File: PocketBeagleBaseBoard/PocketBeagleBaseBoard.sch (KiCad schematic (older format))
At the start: 16 parts, among them J1 RJ45, J2 RJ45, P1 POCKETBEAGLE-P1, P2 POCKETBEAGLE-P2, T1 + 15 in -, T2 + 15 out -, U1 TCAN332DR, U2 SN65HVD233-HT

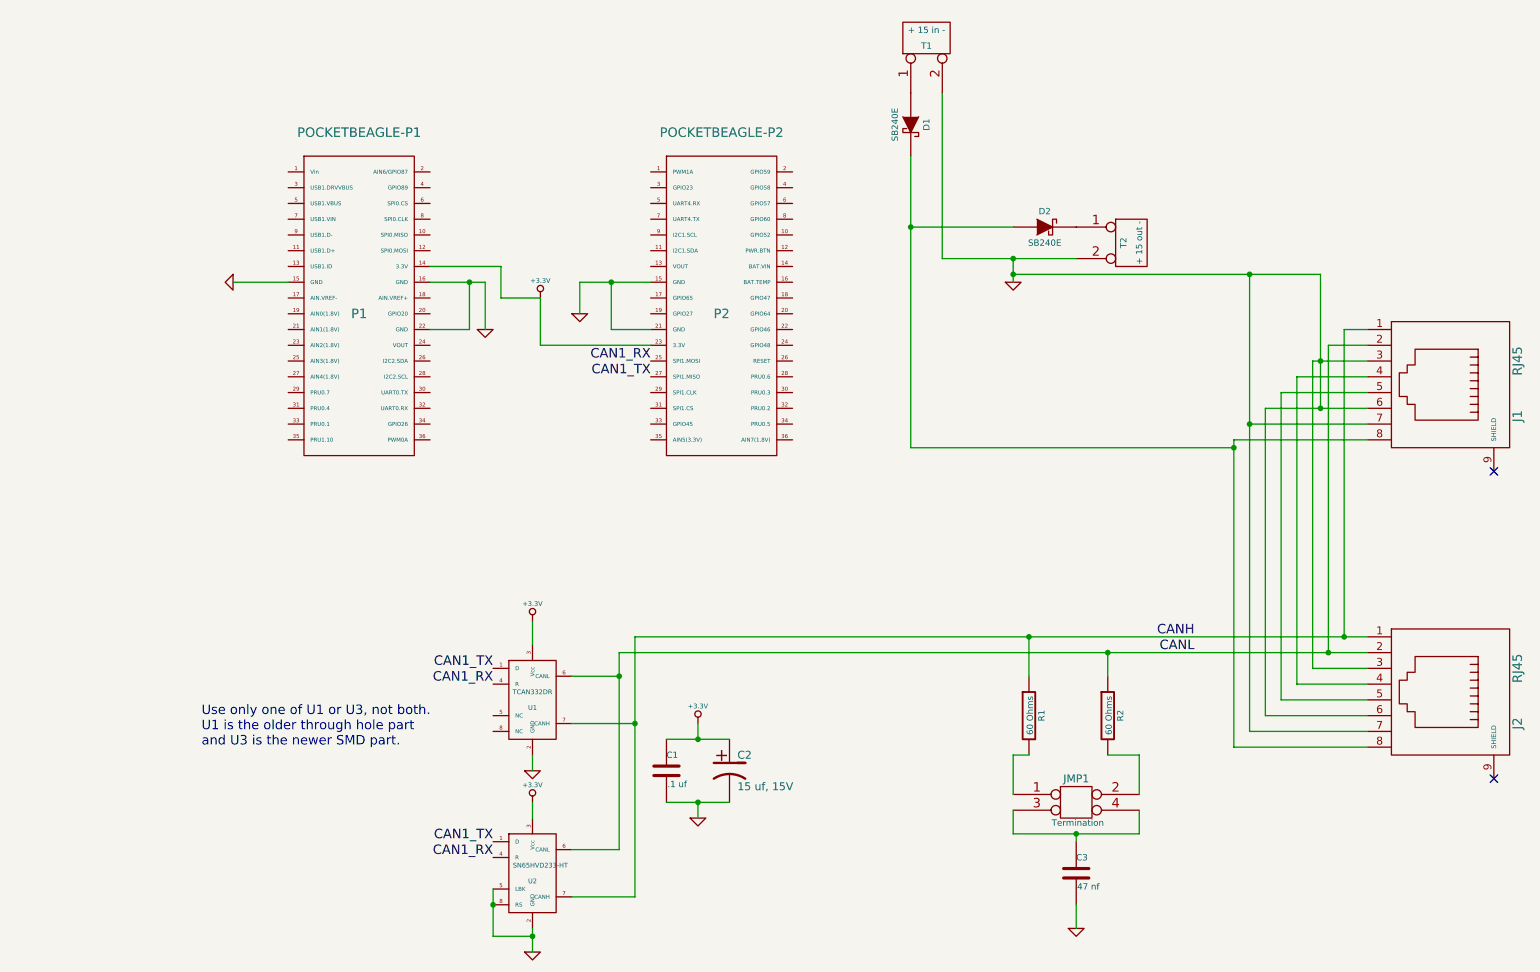
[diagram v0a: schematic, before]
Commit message: Added GPIO, SPI and I2C headers. to PocketBeagleBaseBoard.
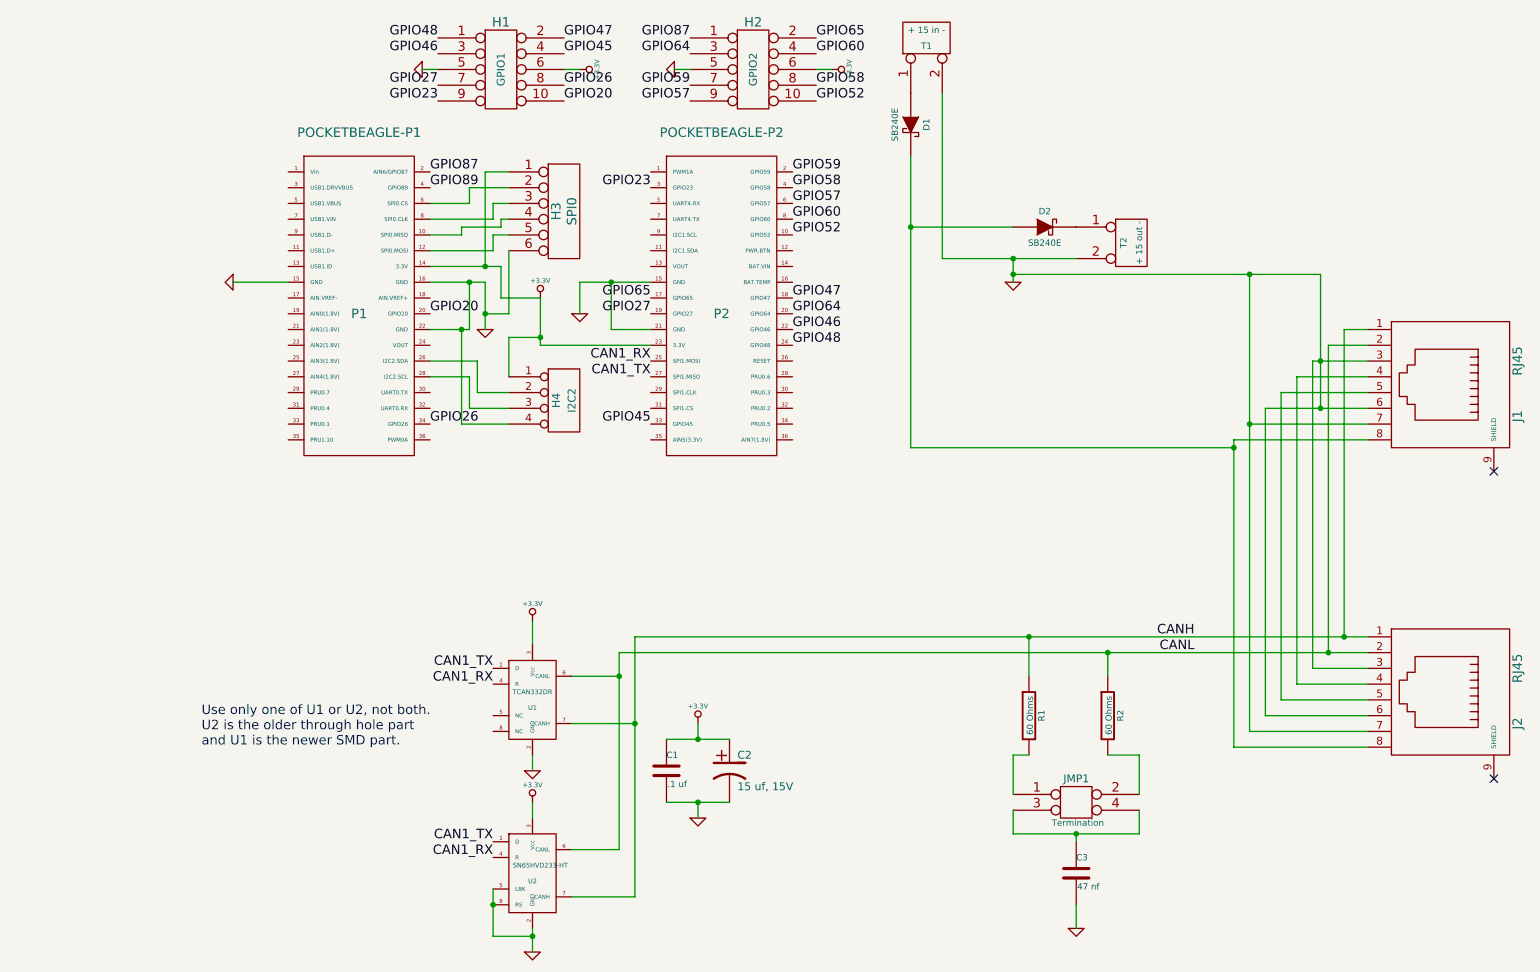
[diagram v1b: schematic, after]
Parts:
- added H1: GPIO1, symbol CONN_5X2
- added H2: GPIO2, symbol CONN_5X2
- added H3: SPI0, symbol CONN_6
- added H4: I2C2, symbol CONN_4
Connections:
- net +3.3V: now also H1.6, H2.6, H3.1, H4.1 (P1)
- net GND: now also H1.5, H2.5, H3.6, H4.4 (P4)
- net at P1.10 (SPI0.MISO): now also H3.4
- net at P1.12 (SPI0.MOSI): now also H3.5
- net GPIO87: now reaches P1.2 (AIN6/GPIO87)
- net GPIO87: now also H2.1
- net GPIO20: now reaches P1.20 (GPIO20)
- net GPIO20: now also H1.10
- net at P1.26 (I2C2.SDA): now also H4.2 (P2)
- net at P1.28 (I2C2.SCL): now also H4.3 (P3)
- net GPIO26: now reaches P1.34 (GPIO26)
- net GPIO26: now also H1.8
- net GPIO89: now reaches P1.4 (GPIO89)
- net at P1.6 (SPI0.CS): now also H3.2
- net at P1.8 (SPI0.CLK): now also H3.3
- net GPIO52: now reaches P2.10 (GPIO52)
- net GPIO52: now also H2.10
- net GPIO65: now reaches P2.17 (GPIO65)
- net GPIO65: now also H2.2
- net GPIO47: now reaches P2.18 (GPIO47)
- net GPIO47: now also H1.2
- net GPIO27: now reaches P2.19 (GPIO27)
- net GPIO27: now also H1.7
- net GPIO59: now reaches P2.2 (GPIO59)
- net GPIO59: now also H2.7
- net GPIO64: now reaches P2.20 (GPIO64)
- net GPIO64: now also H2.3
- net GPIO46: now reaches P2.22 (GPIO46)
- net GPIO46: now also H1.3
- net GPIO48: now reaches P2.24 (GPIO48)
- net GPIO48: now also H1.1
- net GPIO23: now reaches P2.3 (GPIO23)
- net GPIO23: now also H1.9
- net GPIO45: now reaches P2.33 (GPIO45)
- net GPIO45: now also H1.4
- net GPIO58: now reaches P2.4 (GPIO58)
- net GPIO58: now also H2.8
- net GPIO57: now reaches P2.6 (GPIO57)
- net GPIO57: now also H2.9
- net GPIO60: now reaches P2.8 (GPIO60)
- net GPIO60: now also H2.4
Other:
- note added: "Use only one of U1 or U2, not both.\nU2 is the older through hole part\nand U1 is the newer SMD part."
- note removed: "Use only one of U1 or U3, not both.\nU1 is the older through hole part\nand U3 is the newer SMD part."

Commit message: Added a 5V power supply (from CAN power) to PocketBeagleBaseBoard.
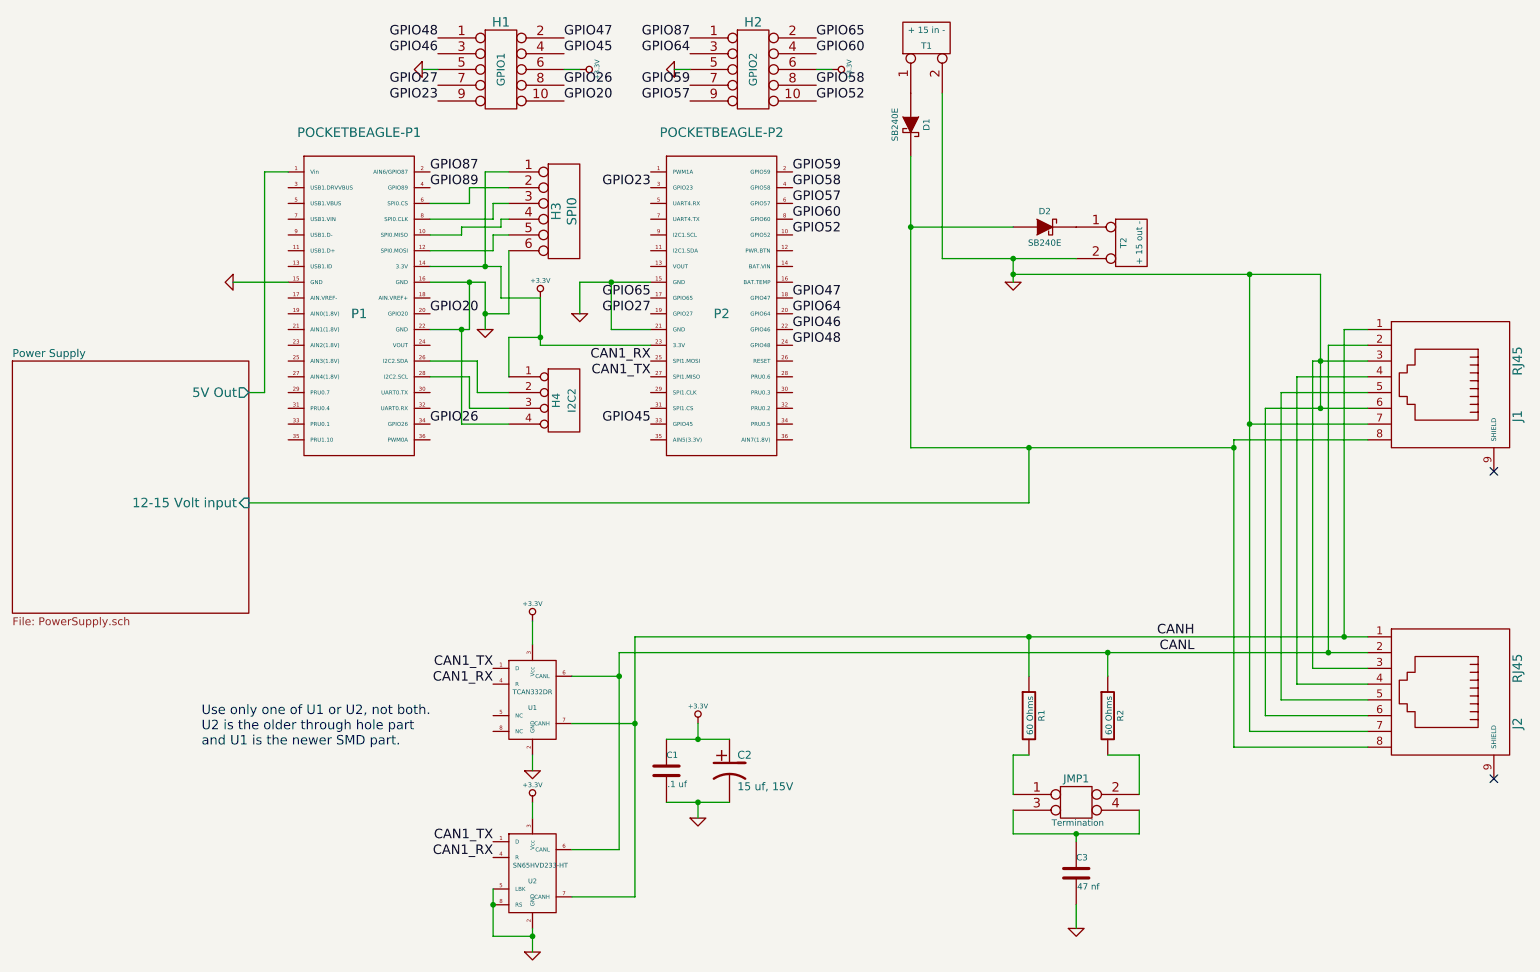
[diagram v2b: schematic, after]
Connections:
- net Power Supply/5V Out: now reaches P1.1 (Vin)
- net Power Supply/12-15 Volt input: now reaches D1.2 (K), D2.1 (A), J1.8, J2.8
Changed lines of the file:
@@
 LIBS:pocketbeagle
 LIBS:sn65hvd233-ht
+LIBS:lm2574n-5
 LIBS:PocketBeagleBaseBoard-cache
 EELAYER 27 0
@@
 $Descr A4 11693 8268
 encoding utf-8
-Sheet 1 1
+Sheet 1 2
 Title ""
 Date "4 mar 2019"
@@
 Wire Wire Line
 	3550 3150 3800 3150
+$Sheet
+S 650  2850 1500 1600
+U 5C7D285B
+F0 "Power Supply" 50
+F1 "PowerSupply.sch" 50
+F2 "5V Out" O R 2150 3050 60
+F3 "12-15 Volt input" I R 2150 3750 60
+$EndSheet
+Wire Wire Line
+	2400 1650 2250 1650
+Wire Wire Line
+	2250 1650 2250 3050
+Wire Wire Line
+	2250 3050 2150 3050
+Wire Wire Line
+	2150 3750 7100 3750
+Wire Wire Line
+	7100 3750 7100 3400
+Connection ~ 7100 3400
 $EndSCHEMATC
